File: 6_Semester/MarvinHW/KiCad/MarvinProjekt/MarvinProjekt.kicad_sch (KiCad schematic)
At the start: 13 parts, among them J1 Conn_02x03_Odd_Even, SW1 SW_DPST_x2, SW2 SW_DPST_x2, U1 ESP32-S3-WROOM-1, X1 USB3.1C16PFSMT

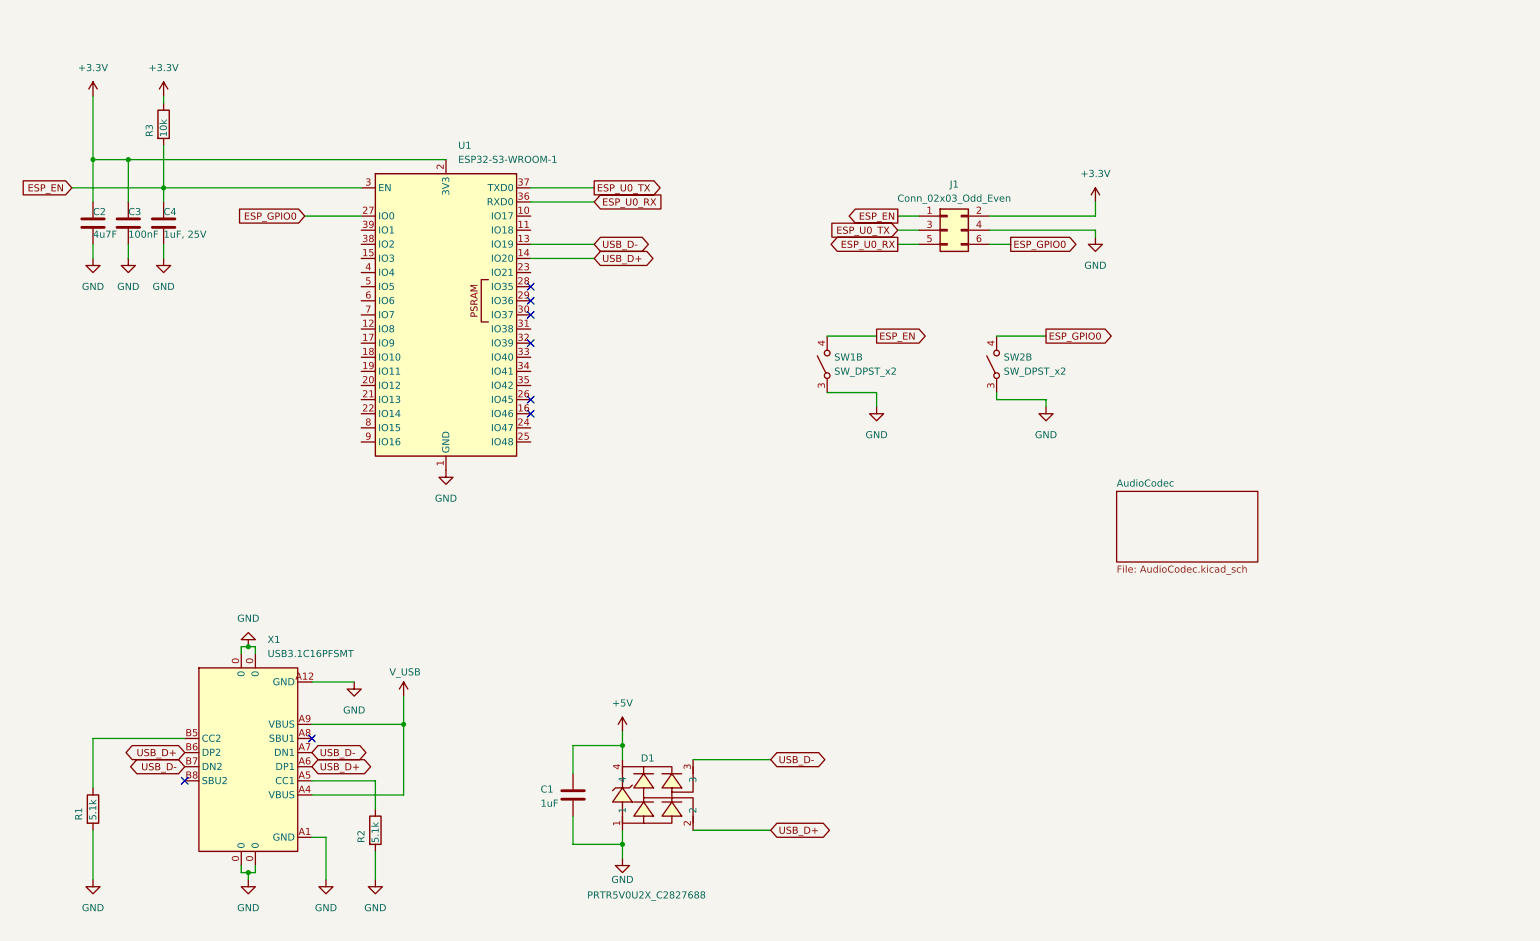
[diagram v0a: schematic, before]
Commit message: made SD-Card, Audio Codec and Amplifier schematic
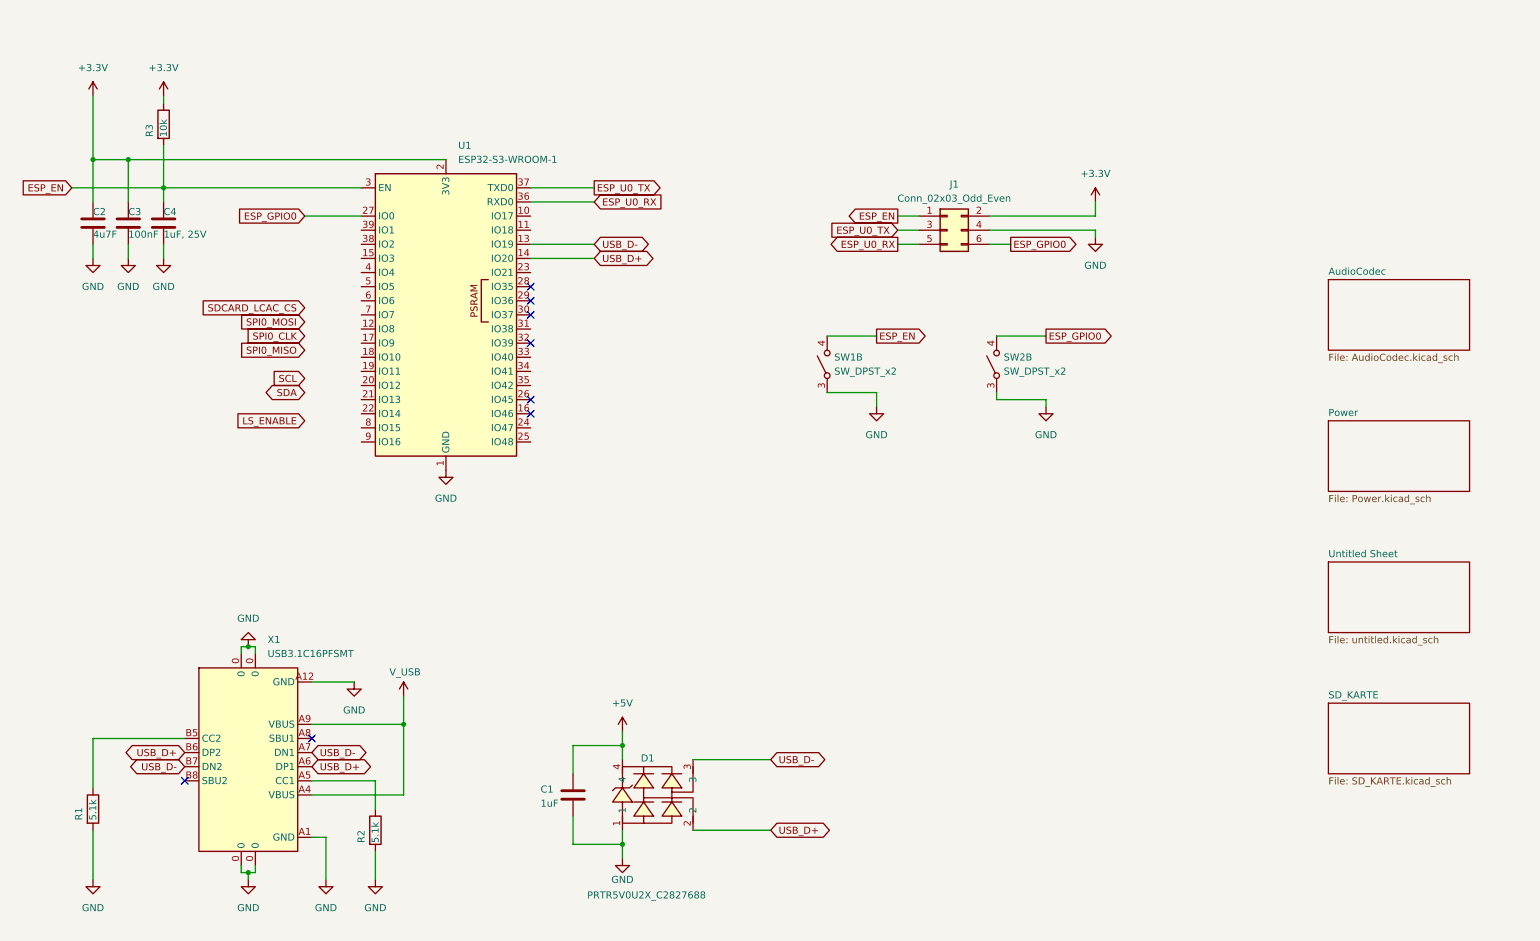
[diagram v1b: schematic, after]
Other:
- added sheet Power (Power.kicad_sch)
- added sheet SD_KARTE (SD_KARTE.kicad_sch)
- added sheet Untitled Sheet (untitled.kicad_sch)

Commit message: added datasheets and worked on schematic
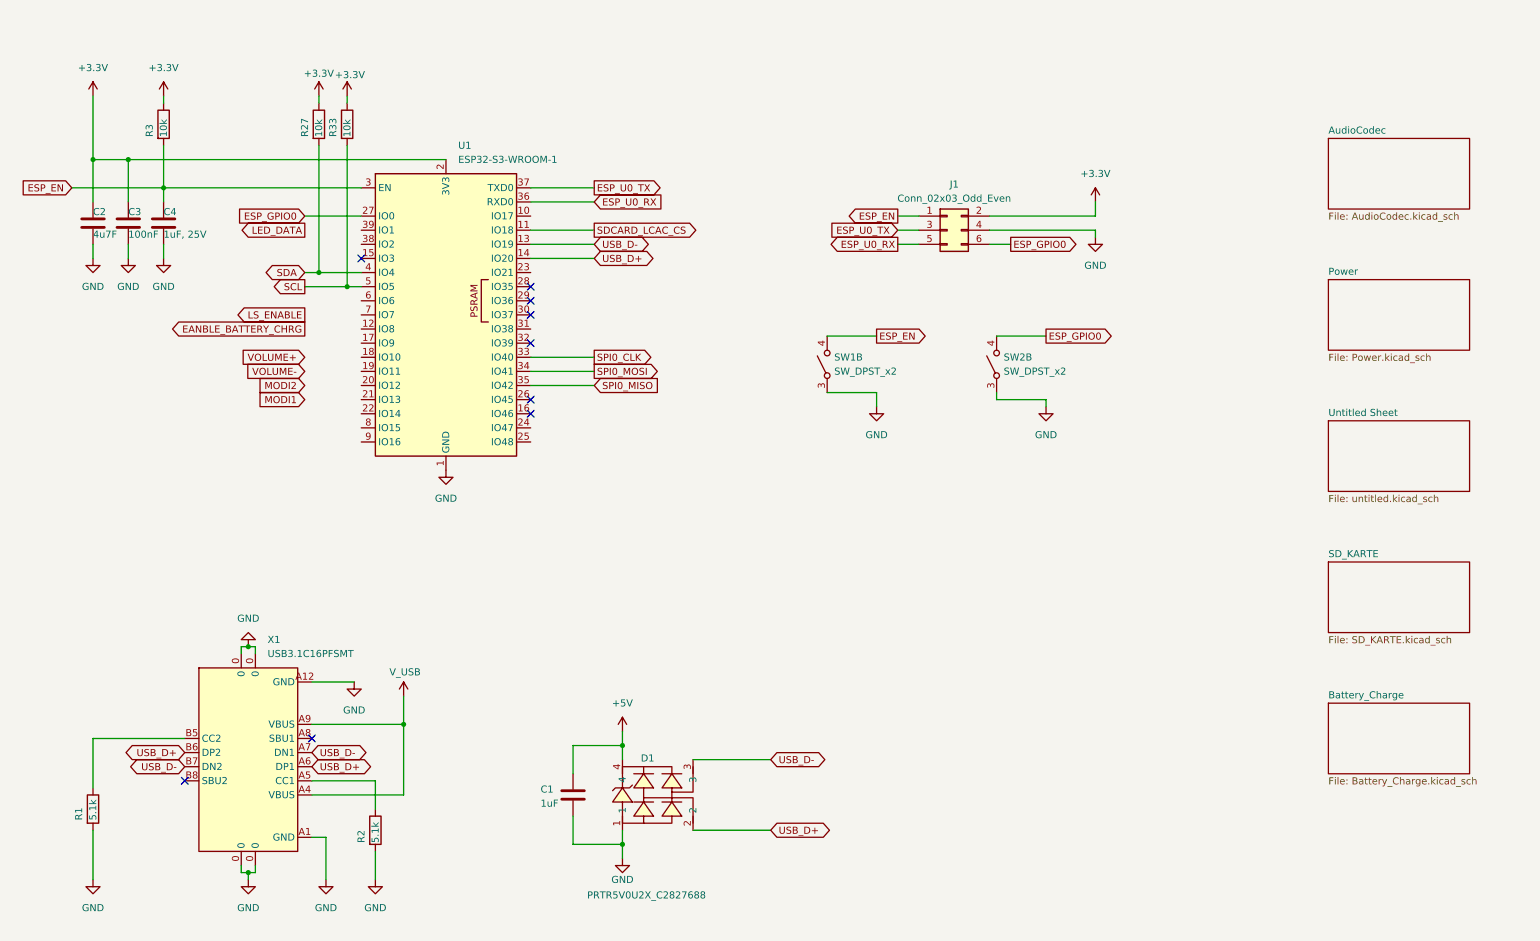
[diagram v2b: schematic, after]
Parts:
- added R27, R33: 10k, Resistor_SMD:R_0805_2012Metric_Pad1.20x1.40mm_HandSolder, symbol Device:R
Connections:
- net +3.3V: now also R27.1, R33.1
- net SCL: now also U1.5 (IO5), R33.2
- net SDA: now also U1.4 (IO4), R27.2
- net SDCARD_LCAC_CS: now also U1.11 (IO18)
- net SPI0_CLK: now also U1.33 (IO40)
- net SPI0_MISO: now also U1.35 (IO42)
- net SPI0_MOSI: now also U1.34 (IO41)
- no-connect marks 8 -> 9
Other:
- added sheet Battery_Charge (Battery_Charge.kicad_sch)

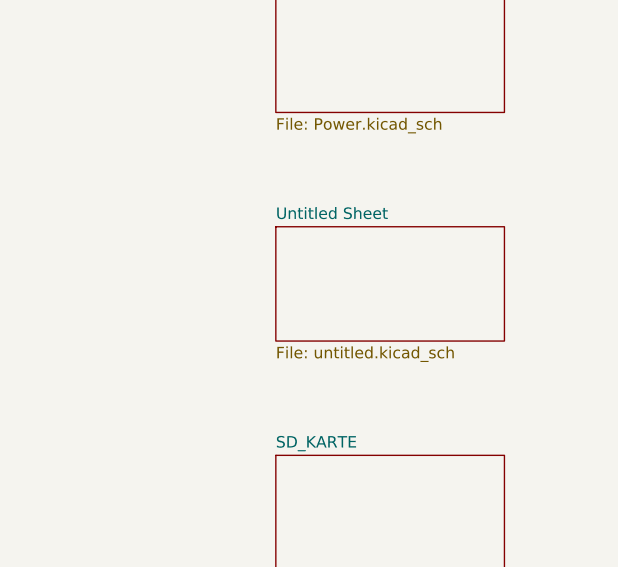
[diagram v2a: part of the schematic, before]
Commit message: renamed untitledsheet to crontrol
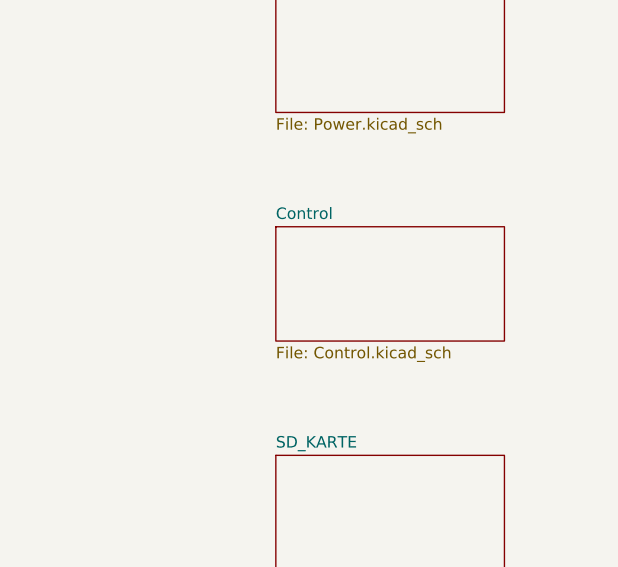
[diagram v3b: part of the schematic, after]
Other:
- sheet Untitled Sheet renamed Control
- sheet Control: file untitled.kicad_sch -> Control.kicad_sch
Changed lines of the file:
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@@
 			(color 0 0 0 0.0000)
 		)
-		(property "Sheetname" "Untitled Sheet"
+		(property "Sheetname" "Control"
 			(at 254 88.1884 0)
 			(effects
@@
 			)
 		)
-		(property "Sheetfile" "untitled.kicad_sch"
+		(property "Sheetfile" "Control.kicad_sch"
 			(at 254 102.1846 0)
 			(effects

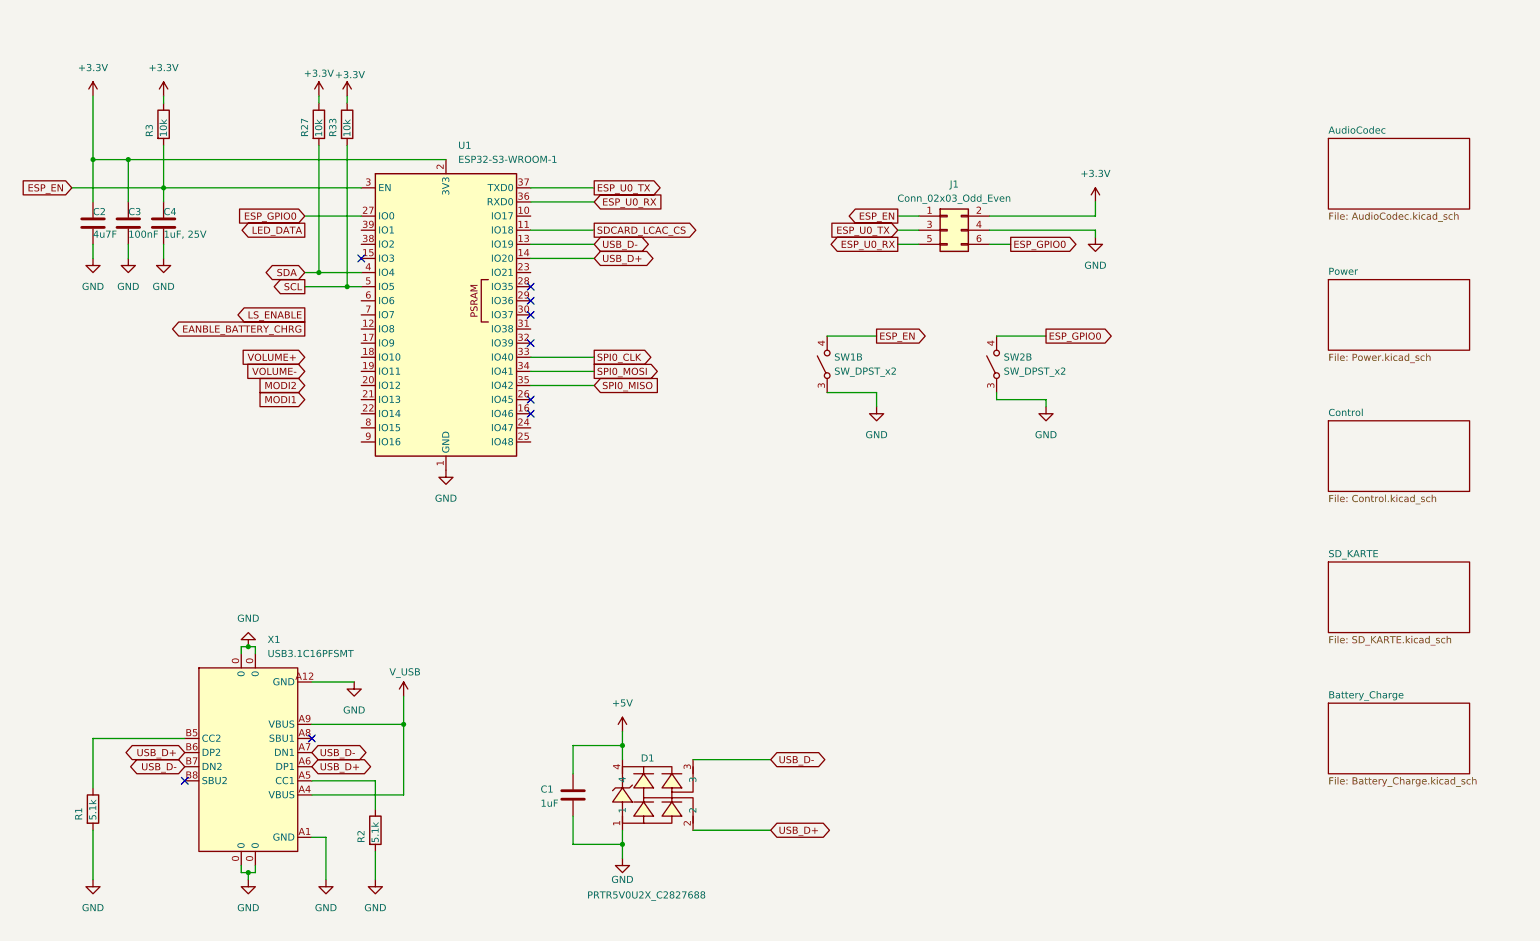
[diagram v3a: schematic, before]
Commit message: finished schematic working on footprints
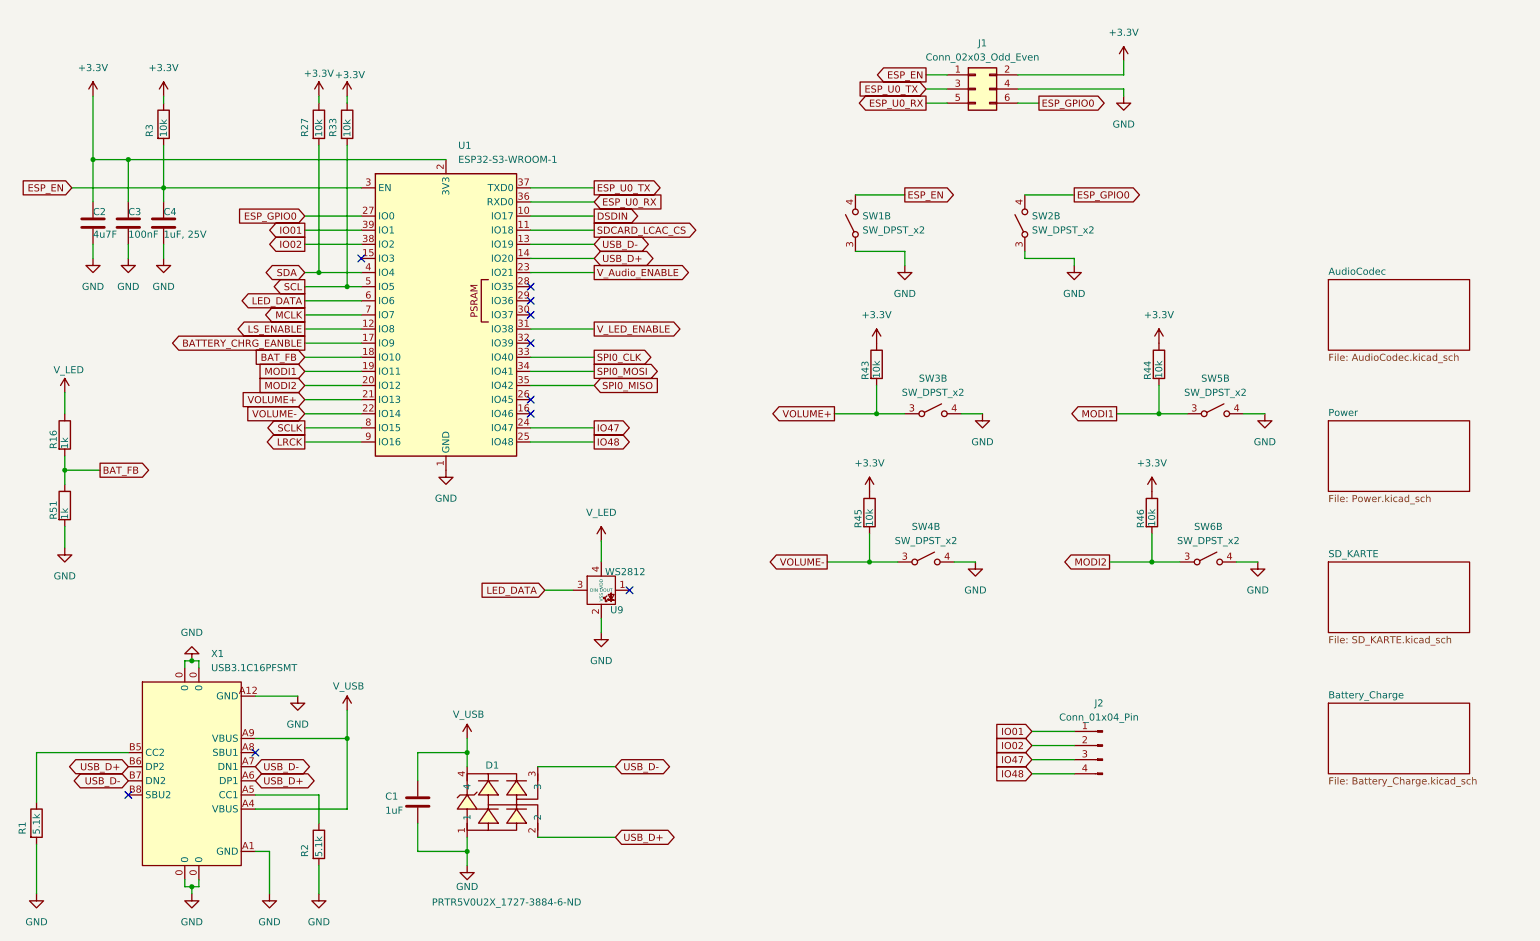
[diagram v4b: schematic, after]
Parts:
- added J2: Conn_01x04_Pin, Connector_PinHeader_2.54mm:PinHeader_1x04_P2.54mm_Vertical, symbol Connector:Conn_01x04_Pin
- added R16, R51: 1k, Resistor_SMD:R_0805_2012Metric_Pad1.20x1.40mm_HandSolder, symbol Device:R
- added R43, R44, R45, R46: 10k, Resistor_SMD:R_0805_2012Metric_Pad1.20x1.40mm_HandSolder, symbol Device:R
- added SW3, SW4, SW5, SW6: SW_DPST_x2, Matrix2_Schnuppiprojekt:Taster, symbol Switch:SW_DPST_x2
- added U9: WS2812, LED_SMD:LED_WS2812B-2020_PLCC4_2.0x2.0mm, symbol Library:WS2812
- D1: value PRTR5V0U2X_C2827688 -> PRTR5V0U2X_1727-3884-6-ND
- U1: footprint Matrix2_Schnuppiprojekt:ESP32-S3-WROOM-1 -> RF_Module:ESP32-S3-WROOM-1
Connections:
- net +5V is gone; now on net V_USB: C1.1, D1.4
- net +3.3V: now also R43.1, R44.1, R45.1, R46.1
- net GND: now also R51.2, SW3.4 (B), SW4.4 (B), SW5.4 (B), SW6.4 (B), U9.2 (VSS)
- net LED_DATA: now also U1.6 (IO6), U9.3 (DIN)
- net LS_ENABLE: now also U1.12 (IO8)
- net MODI1: now also U1.19 (IO11), R44.2, SW5.3 (A)
- net MODI2: now also U1.20 (IO12), R46.2, SW6.3 (A)
- net VOLUME+: now also U1.21 (IO13), R43.2, SW3.3 (A)
- net VOLUME-: now also U1.22 (IO14), R45.2, SW4.3 (A)
- net DSDIN: now reaches U1.10 (IO17)
- net BATTERY_CHRG_EANBLE: now reaches U1.17 (IO9)
- net BAT_FB: now reaches U1.18 (IO10)
- net BAT_FB: now also R16.2, R51.1
- net V_Audio_ENABLE: now reaches U1.23 (IO21)
- net IO47: now reaches U1.24 (IO47)
- net IO47: now also J2.3 (Pin_3)
- net IO48: now reaches U1.25 (IO48)
- net IO48: now also J2.4 (Pin_4)
- net V_LED_ENABLE: now reaches U1.31 (IO38)
- net IO02: now reaches U1.38 (IO2)
- net IO02: now also J2.2 (Pin_2)
- net IO01: now reaches U1.39 (IO1)
- net IO01: now also J2.1 (Pin_1)
- net MCLK: now reaches U1.7 (IO7)
- net SCLK: now reaches U1.8 (IO15)
- net LRCK: now reaches U1.9 (IO16)
- new net V_LED: R16.1, U9.4 (VDD)
- no-connect marks 9 -> 10
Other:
- removed sheet Control
- moved on the sheet: C1, D1, J1, R1, R2, SW1B, SW2B, X1
